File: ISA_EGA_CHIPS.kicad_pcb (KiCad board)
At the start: 2 copper layers, 131.1 x 108 mm, 67 parts, among them J1 EGA Feature Connector, J2 Light Pen, J3 RCA 1, J4 RCA 2, J6 Digital Output, J7 Bus_ISA_8bit, SW1 Configuration, U1 41464, U10 27C256, U11 82A436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

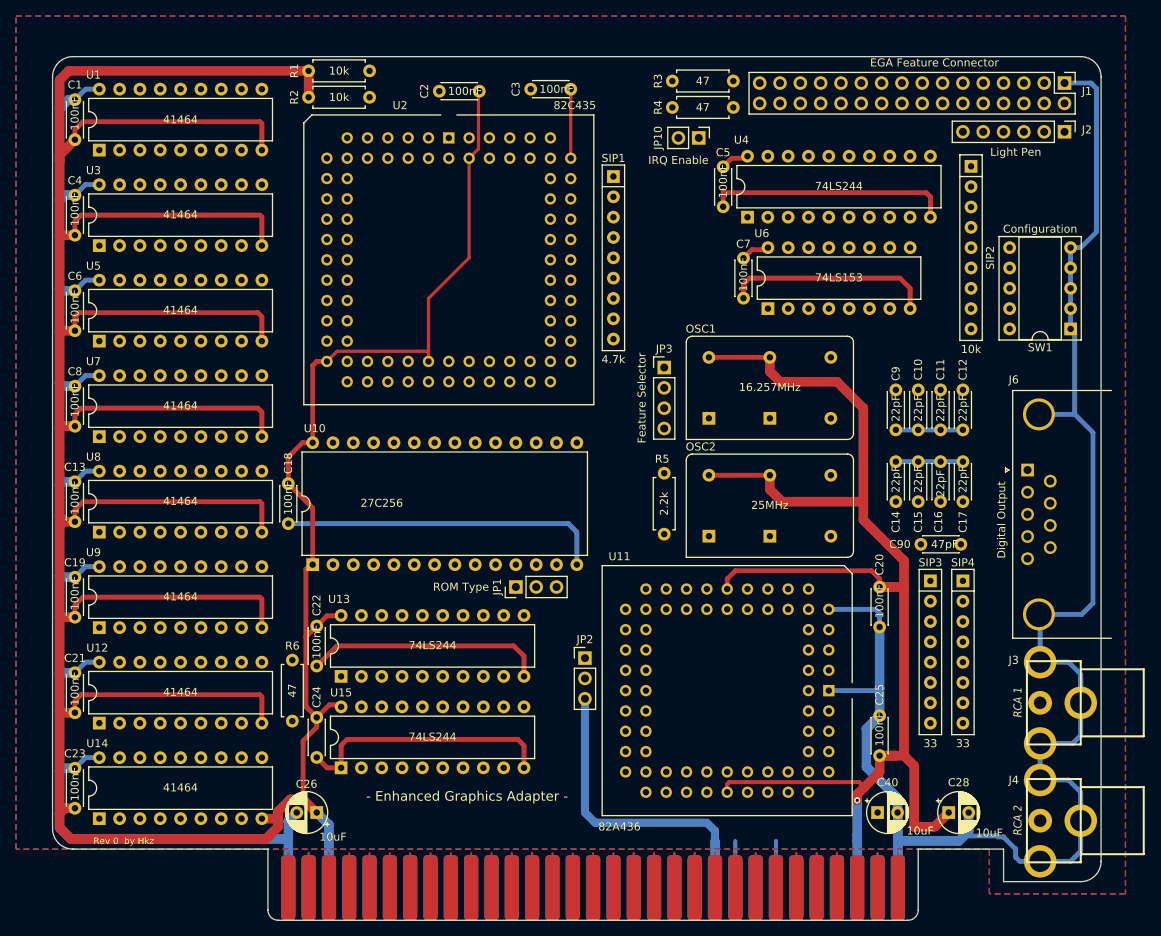
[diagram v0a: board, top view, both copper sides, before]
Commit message: Rerouted power traces
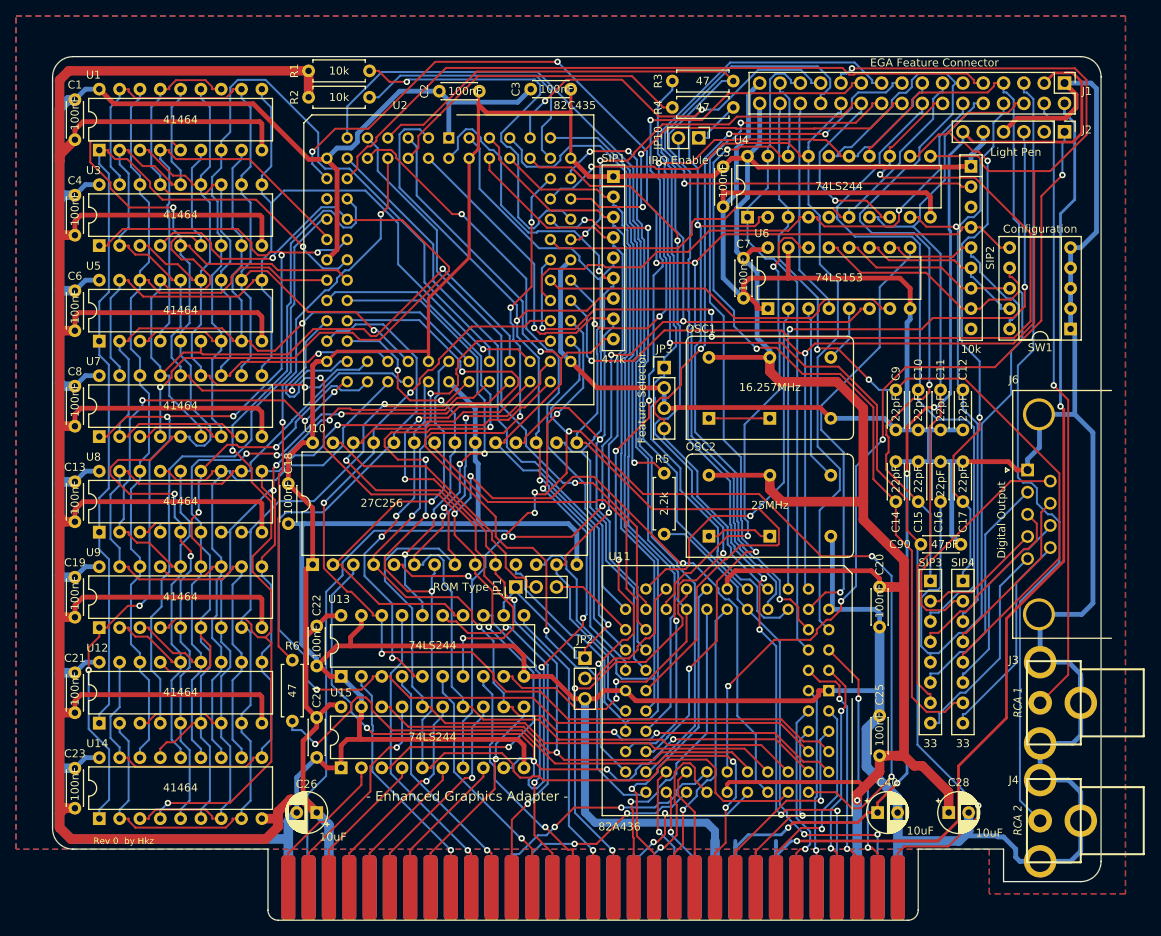
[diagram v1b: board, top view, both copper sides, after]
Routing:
- net GND: track 597.2 -> 949.5 mm
- net /BS_V: track 0.00 -> 187.8 mm, vias 0 -> 5
- net /BUS_OSC: track 4.32 -> 188.0 mm, vias 0 -> 4
- net /BUF_A01: track 0.00 -> 170.8 mm, vias 0 -> 6
- net /IOADS: track 0.00 -> 165.4 mm, vias 0 -> 4
- net /BUF_A07: track 0.00 -> 161.7 mm, vias 0 -> 8
- net /BUF_A05: track 0.00 -> 160.1 mm, vias 0 -> 7
- net /BUF_A03: track 0.00 -> 156.0 mm, vias 0 -> 4
- net /~RAS: track 0.00 -> 151.1 mm, vias 0 -> 3
- net /BUF_A00: track 0.00 -> 143.1 mm, vias 0 -> 5
- net /BUF_A15: track 0.00 -> 138.4 mm, vias 0 -> 2
- net +12V: track 5.84 -> 143.8 mm, vias 0 -> 4
- net /BUF_A09: track 0.00 -> 133.9 mm, vias 0 -> 1
- net /~DRAM_OE13: track 0.00 -> 133.3 mm, vias 0 -> 6
- net Net-(C90-Pad2): track 4.32 -> 136.5 mm, vias 0 -> 2
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
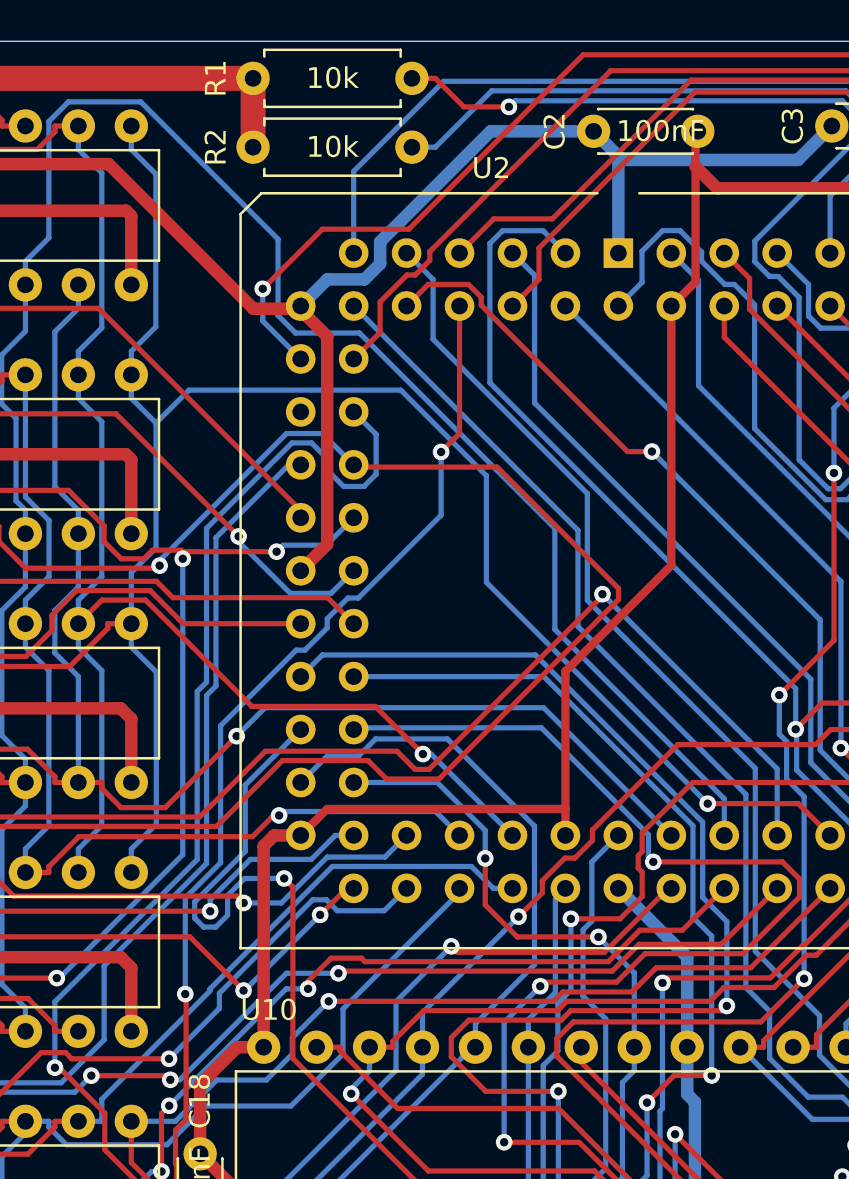
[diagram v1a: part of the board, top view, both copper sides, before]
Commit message: redraw some traces
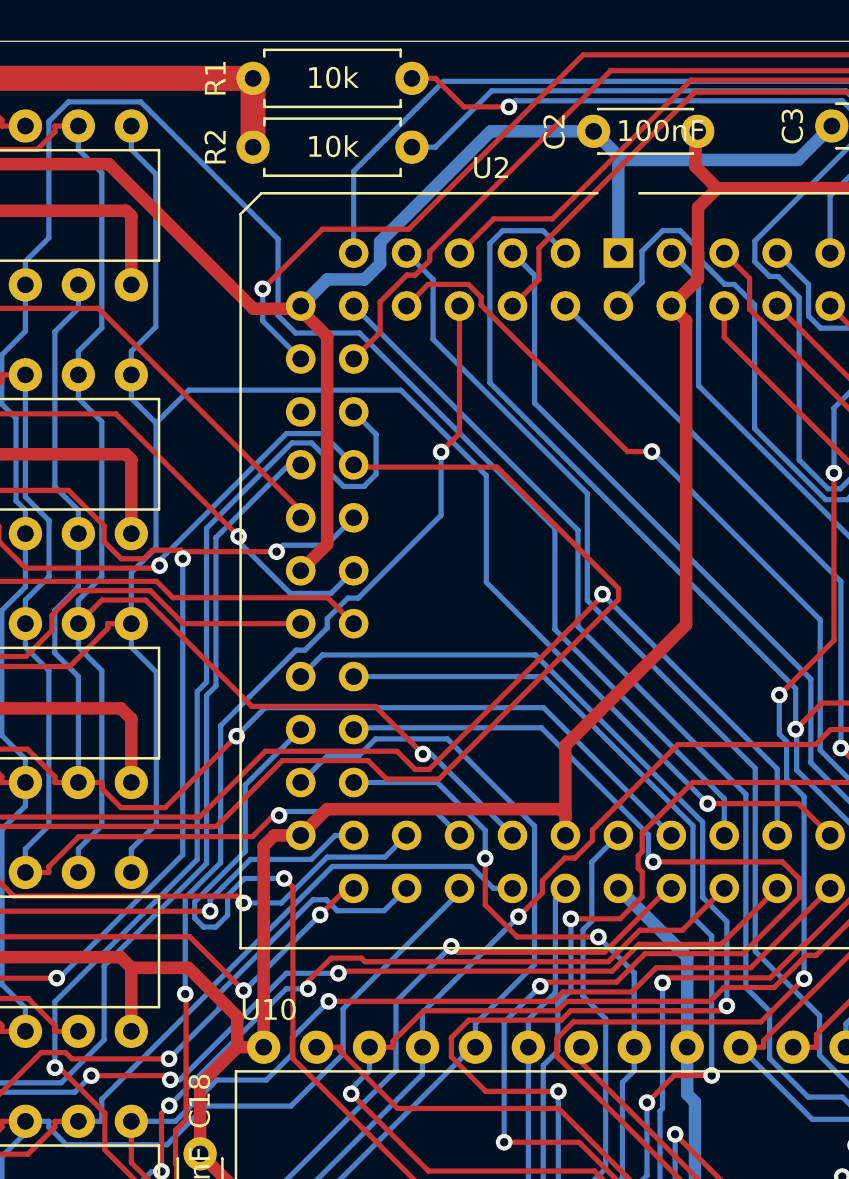
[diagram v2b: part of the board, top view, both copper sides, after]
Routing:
- net VCC: track 800.3 -> 809.4 mm
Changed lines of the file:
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@@
     (thickness 1.6)
     (drawings 22)
-    (tracks 3983)
+    (tracks 3991)
     (zones 0)
     (modules 67)
@@
   )
   (setup
-    (last_trace_width 1.2)
+    (last_trace_width 0.6)
     (user_trace_width 0.4)
     (user_trace_width 0.5)
@@
   (segment (start 272.288 101.346) (end 272.288 102.7463) (width 0.6) (layer B.Cu) (net 2))
   (segment (start 290.322 182.88) (end 289.306 182.88) (width 1.2) (layer F.Cu) (net 2))
-  (segment (start 237.127 101.5165) (end 237.127 99.9308) (width 0.4) (layer F.Cu) (net 2))
   (segment (start 237.127 99.9308) (end 237.236 99.822) (width 0.4) (layer F.Cu) (net 2))
-  (segment (start 235.966 108.204) (end 237.127 107.043) (width 0.4) (layer F.Cu) (net 2))
-  (segment (start 237.127 107.043) (end 237.127 101.5165) (width 0.4) (layer F.Cu) (net 2))
   (segment (start 184.771 177.405) (end 184.771 165.467) (width 1.2) (layer F.Cu) (net 2))
   (segment (start 186.69 177.516) (end 184.882 177.516) (width 1.2) (layer F.Cu) (net 2))
@@
   (segment (start 287.274 183.388) (end 287.274 182.88) (width 0.4) (layer F.Cu) (net 2))
   (segment (start 230.886 133.604) (end 230.886 132.334) (width 0.4) (layer F.Cu) (net 2))
-  (segment (start 230.886 132.334) (end 219.456 132.334) (width 0.4) (layer F.Cu) (net 2))
-  (segment (start 219.456 132.334) (end 218.186 133.604) (width 0.4) (layer F.Cu) (net 2))
-  (segment (start 230.886 132.334) (end 230.886 125.73) (width 0.4) (layer F.Cu) (net 2))
-  (segment (start 230.886 125.73) (end 235.966 120.65) (width 0.4) (layer F.Cu) (net 2))
-  (segment (start 235.966 120.65) (end 235.966 108.204) (width 0.4) (layer F.Cu) (net 2))
   (segment (start 273.558 147.828) (end 265.938 147.828) (width 0.6) (layer F.Cu) (net 2))
   (segment (start 273.558 133.096) (end 265.938 133.096) (width 0.6) (layer F.Cu) (net 2))
@@
   (segment (start 295.91 187.452) (end 295.91 189.992) (width 1.2) (layer F.Cu) (net 2))
   (segment (start 292.608 184.15) (end 295.91 187.452) (width 1.2) (layer F.Cu) (net 2))
+  (segment (start 237.244799 106.925201) (end 235.966 108.204) (width 0.6) (layer F.Cu) (net 2))
+  (segment (start 237.244799 103.480301) (end 237.244799 106.925201) (width 0.6) (layer F.Cu) (net 2))
+  (segment (start 238.1678 102.5573) (end 237.244799 103.480301) (width 0.6) (layer F.Cu) (net 2))
+  (segment (start 237.127 99.931) (end 237.236 99.822) (width 0.6) (layer F.Cu) (net 2))
+  (segment (start 237.127 101.5165) (end 237.127 99.931) (width 0.6) (layer F.Cu) (net 2))
+  (segment (start 236.677199 108.915199) (end 236.677199 123.494801) (width 0.6) (layer F.Cu) (net 2))
+  (segment (start 235.966 108.204) (end 236.677199 108.915199) (width 0.6) (layer F.Cu) (net 2))
+  (segment (start 236.677199 123.494801) (end 230.886 129.286) (width 0.6) (layer F.Cu) (net 2))
+  (segment (start 219.447201 132.342799) (end 218.186 133.604) (width 0.6) (layer F.Cu) (net 2))
+  (segment (start 230.640799 132.342799) (end 219.447201 132.342799) (width 0.6) (layer F.Cu) (net 2))
+  (segment (start 230.886 132.588) (end 230.640799 132.342799) (width 0.6) (layer F.Cu) (net 2))
+  (segment (start 230.886 129.286) (end 230.886 132.588) (width 0.6) (layer F.Cu) (net 2))
+  (segment (start 230.886 132.588) (end 230.886 133.604) (width 0.6) (layer F.Cu) (net 2))
+  (segment (start 215.138 142.299298) (end 215.138 143.764) (width 0.6) (layer F.Cu) (net 2))
+  (segment (start 212.792702 139.954) (end 215.138 142.299298) (width 0.6) (layer F.Cu) (net 2))
+  (segment (start 210.058 139.954) (end 212.792702 139.954) (width 0.6) (layer F.Cu) (net 2))
   (segment (start 297.688 170.0707) (end 297.8752 170.0707) (width 0.25) (layer F.Cu) (net 3))
   (segment (start 297.8752 170.0707) (end 309.7495 158.1964) (width 0.25) (layer F.Cu) (net 3))

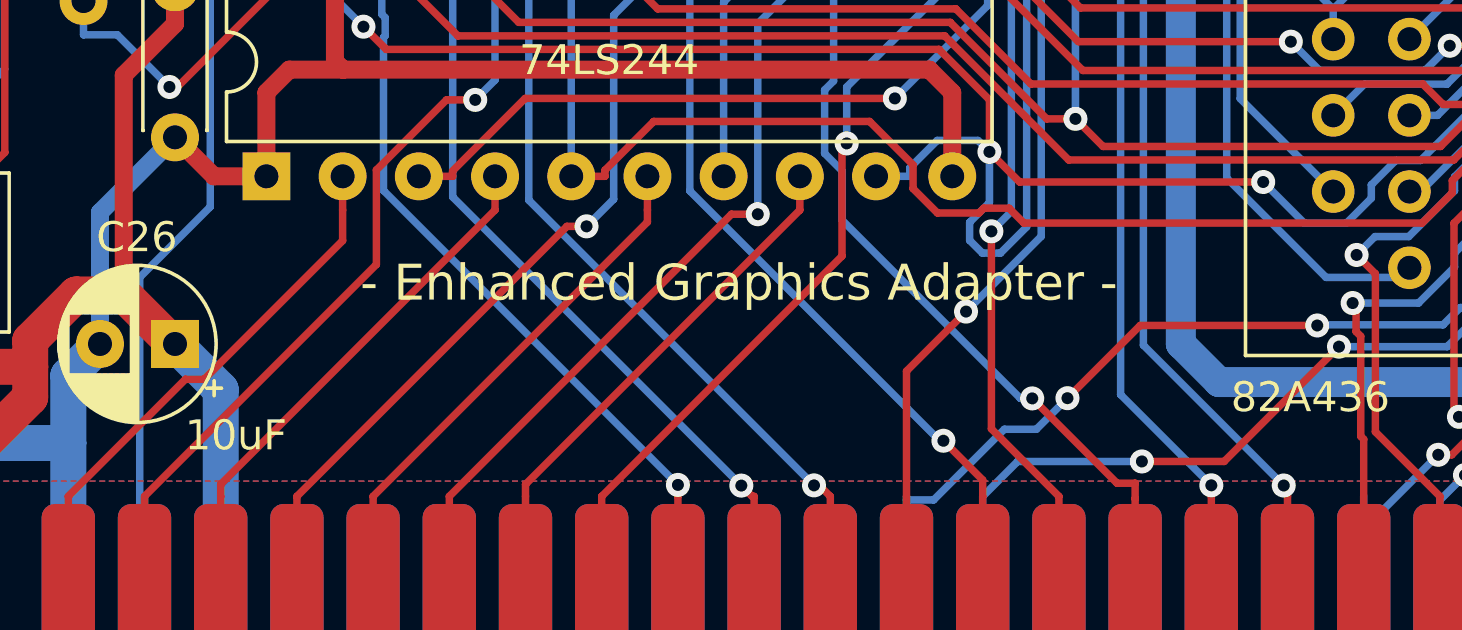
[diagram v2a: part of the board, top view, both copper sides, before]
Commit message: Changed silkscreen
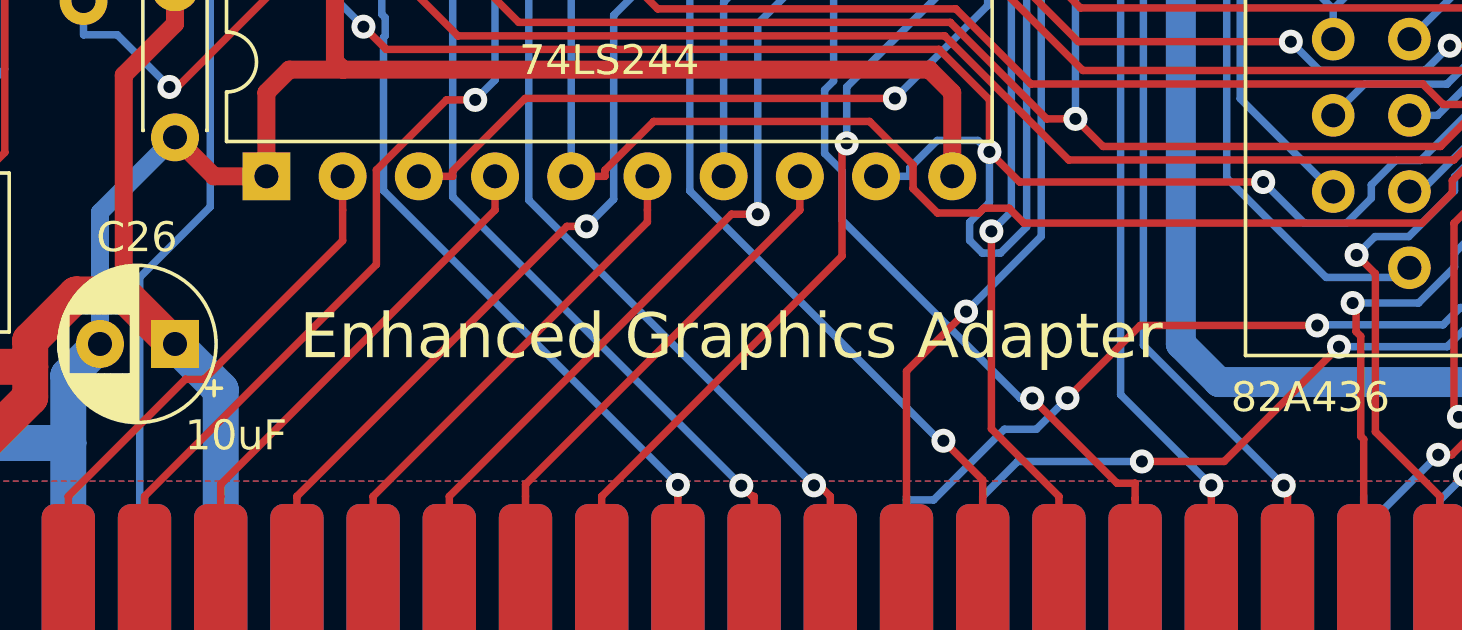
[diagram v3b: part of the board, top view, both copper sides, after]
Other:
- board text added: "Enhanced Graphics Adapter"
- board text removed: "- Enhanced Graphics Adapter -"
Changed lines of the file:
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@@
     (effects (font (size 0.8 0.8) (thickness 0.15)))
   )
-  (gr_text "- Enhanced Graphics Adapter -\n" (at 235.712 187.96) (layer F.SilkS)
-    (effects (font (size 1.2 1.2) (thickness 0.3)))
+  (gr_text "Enhanced Graphics Adapter" (at 235.458 189.738) (layer F.SilkS)
+    (effects (font (size 1.5 1.5) (thickness 0.3)))
   )
   (dimension 22.098 (width 0.15) (layer Dwgs.User)
